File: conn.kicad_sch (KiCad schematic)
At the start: 31 parts, among them J1 JST_1x02, J10 MicroFit_2x04, J11 MLX_1x03, J12 MLX_1x03, J13 JST_1x04, J14 JST_1x04, J15 JST_1x04, J16 JST_1x04, J17 JST_1x02, J7 JST_B6B-XH, J8 MicroFit_2x04, J9 MicroFit_2x04, SW2 !EMERG STOP!

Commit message: Lots of changes and errors fixed. Updated vanity images.
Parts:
- added J5: JST_01x02, Connector_JST:JST_EH_B2B-EH-A_1x02_P2.50mm_Vertical, symbol Connector_Generic:Conn_01x02
- added NT3, NT9: DNI, _footprints:NetTie-2_SMD_Pad0.3mm, symbol Device:NetTie_2
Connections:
- net P1_OUT renamed XMIN_OUT
- net P2_OUT renamed YMIN_OUT
- net P3_OUT renamed ZMIN_OUT
- net P4_OUT renamed PROBE_OUT
- new net P16_IN: NT3.1
- new net P16_OUT: J5.1 (Pin_1), NT3.2
- new net P17_IN: NT9.1
- new net P17_OUT: J5.2 (Pin_2), NT9.2
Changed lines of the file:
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@@
     (rev "1.0")
+  )
+  (junction (at 215.9 82.55) (diameter 0) (color 0 0 0 0)
+  )
+  (junction (at 215.9 85.09) (diameter 0) (color 0 0 0 0)
   )
   (no_connect (at 162.56 52.07))
@@
     (stroke (width 0) (type default) (color 0 0 0 0))
   )
+  (wire (pts (xy 215.9 80.01) (xy 215.9 82.55))
+    (stroke (width 0) (type default) (color 0 0 0 0))
+  )
   (wire (pts (xy 182.245 58.42) (xy 182.245 57.15))
     (stroke (width 0) (type default) (color 0 0 0 0))
@@
     (stroke (width 0) (type default) (color 0 0 0 0))
   )
+  (wire (pts (xy 217.17 80.01) (xy 215.9 80.01))
+    (stroke (width 0) (type default) (color 0 0 0 0))
+  )
   (wire (pts (xy 56.515 77.47) (xy 59.055 77.47))
     (stroke (width 0) (type default) (color 0 0 0 0))
@@
     (stroke (width 0) (type default) (color 0 0 0 0))
   )
+  (wire (pts (xy 215.9 85.09) (xy 218.44 85.09))
+    (stroke (width 0) (type default) (color 0 0 0 0))
+  )
   (wire (pts (xy 64.135 87.63) (xy 66.675 87.63))
     (stroke (width 0) (type default) (color 0 0 0 0))
@@
     (stroke (width 0) (type default) (color 0 0 0 0))
   )
+  (wire (pts (xy 208.28 82.55) (xy 210.82 82.55))
+    (stroke (width 0) (type default) (color 0 0 0 0))
+  )
   (wire (pts (xy 56.515 56.515) (xy 59.055 56.515))
     (stroke (width 0) (type default) (color 0 0 0 0))
@@
     (stroke (width 0) (type default) (color 0 0 0 0))
   )
+  (wire (pts (xy 208.28 85.09) (xy 210.82 85.09))
+    (stroke (width 0) (type default) (color 0 0 0 0))
+  )
   (wire (pts (xy 64.135 107.95) (xy 93.345 107.95))
     (stroke (width 0) (type default) (color 0 0 0 0))
   )
+  (wire (pts (xy 215.9 88.9) (xy 215.9 85.09))
+    (stroke (width 0) (type default) (color 0 0 0 0))
+  )
   (polyline (pts (xy 217.805 138.43) (xy 186.69 138.43))
     (stroke (width 0) (type default) (color 0 0 0 0))
@@
     (stroke (width 0) (type default) (color 0 0 0 0))
   )
+  (wire (pts (xy 217.17 88.9) (xy 215.9 88.9))
+    (stroke (width 0) (type default) (color 0 0 0 0))
+  )
   (wire (pts (xy 116.84 54.61) (xy 119.38 54.61))
     (stroke (width 0) (type default) (color 0 0 0 0))
@@
   )
   (wire (pts (xy 56.515 107.95) (xy 59.055 107.95))
+    (stroke (width 0) (type default) (color 0 0 0 0))
+  )
+  (wire (pts (xy 215.9 82.55) (xy 218.44 82.55))
     (stroke (width 0) (type default) (color 0 0 0 0))
   )
@@
     (effects (font (size 1.27 1.27)) (justify left bottom))
   )
+  (label "P16_OUT" (at 217.17 80.01 0)
+    (effects (font (size 1.27 1.27)) (justify left bottom))
+  )
   (label "XMIN" (at 66.675 51.435 0)
     (effects (font (size 1.27 1.27)) (justify left bottom))
@@
     (effects (font (size 1.27 1.27)) (justify right bottom))
   )
+  (label "P17_OUT" (at 217.17 88.9 0)
+    (effects (font (size 1.27 1.27)) (justify left bottom))
+  )
   (label "XDIR" (at 88.9 87.63 180)
     (effects (font (size 1.27 1.27)) (justify right bottom))
@@
     (effects (font (size 1.27 1.27)) (justify right))
   )
+  (hierarchical_label "P16_IN" (shape input) (at 208.28 82.55 180)
+    (effects (font (size 1.27 1.27)) (justify right))
+  )
+  (hierarchical_label "P17_IN" (shape input) (at 208.28 85.09 180)
+    (effects (font (size 1.27 1.27)) (justify right))
+  )
   (hierarchical_label "ZCLK_IN" (shape input) (at 56.515 87.63 180)
     (effects (font (size 1.27 1.27)) (justify right))
@@
     (effects (font (size 1.27 1.27)) (justify right))
   )
-  (hierarchical_label "P2_OUT" (shape output) (at 56.515 53.975 180)
+  (hierarchical_label "YMIN_OUT" (shape output) (at 56.515 53.975 180)
     (effects (font (size 1.27 1.27)) (justify right))
   )
@@
     (effects (font (size 1.27 1.27)) (justify right))
   )
-  (hierarchical_label "P3_OUT" (shape output) (at 56.515 56.515 180)
-    (effects (font (size 1.27 1.27)) (justify right))
-  )
-  (hierarchical_label "P1_OUT" (shape output) (at 56.515 51.435 180)
+  (hierarchical_label "ZMIN_OUT" (shape output) (at 56.515 56.515 180)
+    (effects (font (size 1.27 1.27)) (justify right))
+  )
+  (hierarchical_label "XMIN_OUT" (shape output) (at 56.515 51.435 180)
     (effects (font (size 1.27 1.27)) (justify right))
   )
@@
     (effects (font (size 1.27 1.27)) (justify right))
   )
-  (hierarchical_label "P4_OUT" (shape output) (at 56.515 59.055 180)
+  (hierarchical_label "PROBE_OUT" (shape output) (at 56.515 59.055 180)
     (effects (font (size 1.27 1.27)) (justify right))
   )
@@
     )
     (pin "1")
+  )
+  (symbol (lib_id "Device:NetTie_2") (at 213.36 82.55 0) (unit 1)
+    (in_bom yes) (on_board yes)
+    (property "Reference" "NT3" (id 0) (at 213.36 81.915 0)
+      (effects (font (size 0.8 0.8)))
+    )
+    (property "Value" "DNI" (id 1) (at 213.36 80.01 0)
+      (effects (font (size 1.27 1.27)) hide)
+    )
+    (property "Footprint" "_footprints:NetTie-2_SMD_Pad0.3mm" (id 2) (at 213.36 82.55 0)
+      (effects (font (size 1.27 1.27)) hide)
+    )
+    (property "Datasheet" "~" (id 3) (at 213.36 82.55 0)
+      (effects (font (size 1.27 1.27)) hide)
+    )
+    (pin "1")
+    (pin "2")
   )
   (symbol (lib_id "Device:NetTie_2") (at 61.595 51.435 0) (unit 1)
@@
     (pin "4")
   )
+  (symbol (lib_id "Connector_Generic:Conn_01x02") (at 223.52 82.55 0) (unit 1)
+    (in_bom yes) (on_board yes) (fields_autoplaced)
+    (property "Reference" "J5" (id 0) (at 226.06 83.8199 0)
+      (effects (font (size 1.27 1.27)) (justify left))
+    )
+    (property "Value" "JST_01x02" (id 1) (at 226.06 85.0899 0)
+      (effects (font (size 1.27 1.27)) (justify left) hide)
+    )
+    (property "Footprint" "Connector_JST:JST_EH_B2B-EH-A_1x02_P2.50mm_Vertical" (id 2) (at 223.52 82.55 0)
+      (effects (font (size 1.27 1.27)) hide)
+    )
+    (property "Datasheet" "~" (id 3) (at 223.52 82.55 0)
+      (effects (font (size 1.27 1.27)) hide)
+    )
+    (property "JLCPCB" "C474892" (id 4) (at 223.52 82.55 0)
+      (effects (font (size 1.27 1.27)) hide)
+    )
+    (property "M.Part#" "KF350-3.5-2P" (id 5) (at 223.52 82.55 0)
+      (effects (font (size 1.27 1.27)) hide)
+    )
+    (property "Manufacturer" "Cixi Kefa Elec" (id 6) (at 223.52 82.55 0)
+      (effects (font (size 1.27 1.27)) hide)
+    )
+    (pin "1")
+    (pin "2")
+  )
   (symbol (lib_id "power:GND") (at 73.66 158.115 0) (unit 1)
     (in_bom yes) (on_board yes)
@@
     (pin "1")
   )
+  (symbol (lib_id "Device:NetTie_2") (at 213.36 85.09 0) (unit 1)
+    (in_bom yes) (on_board yes)
+    (property "Reference" "NT9" (id 0) (at 213.36 84.455 0)
+      (effects (font (size 0.8 0.8)))
+    )
+    (property "Value" "DNI" (id 1) (at 213.36 82.55 0)
+      (effects (font (size 1.27 1.27)) hide)
+    )
+    (property "Footprint" "_footprints:NetTie-2_SMD_Pad0.3mm" (id 2) (at 213.36 85.09 0)
+      (effects (font (size 1.27 1.27)) hide)
+    )
+    (property "Datasheet" "~" (id 3) (at 213.36 85.09 0)
+      (effects (font (size 1.27 1.27)) hide)
+    )
+    (pin "1")
+    (pin "2")
+  )
   (symbol (lib_id "Device:NetTie_2") (at 61.595 53.975 0) (unit 1)

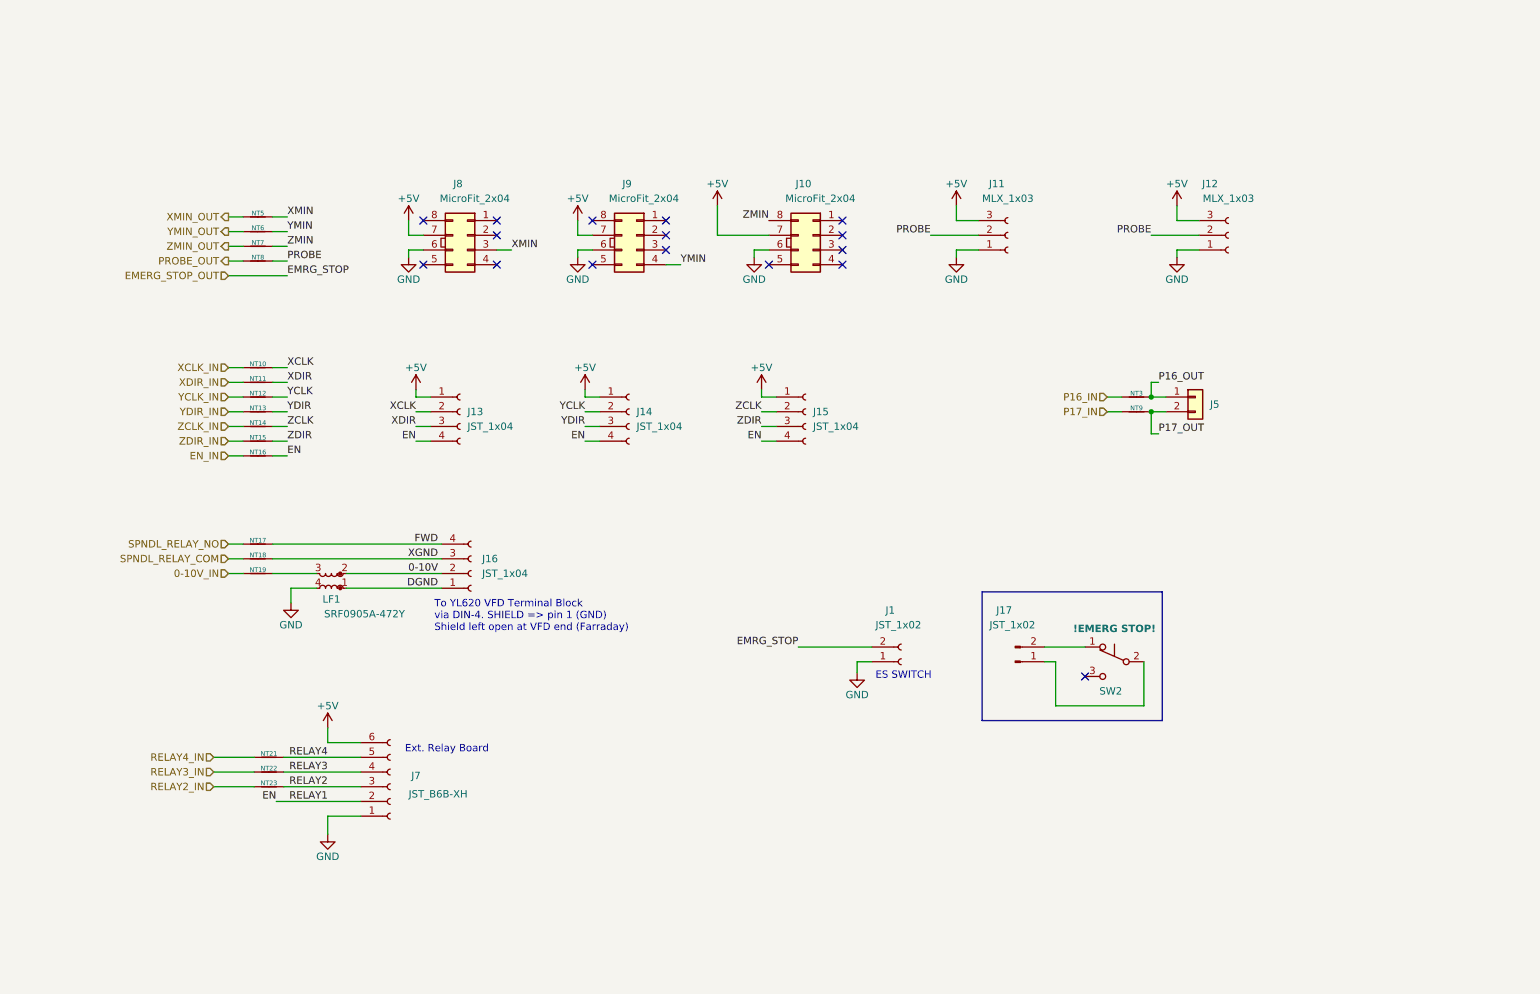
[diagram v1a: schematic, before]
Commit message: Probe connectors wired wrong. Improved 5V buck reg layout.
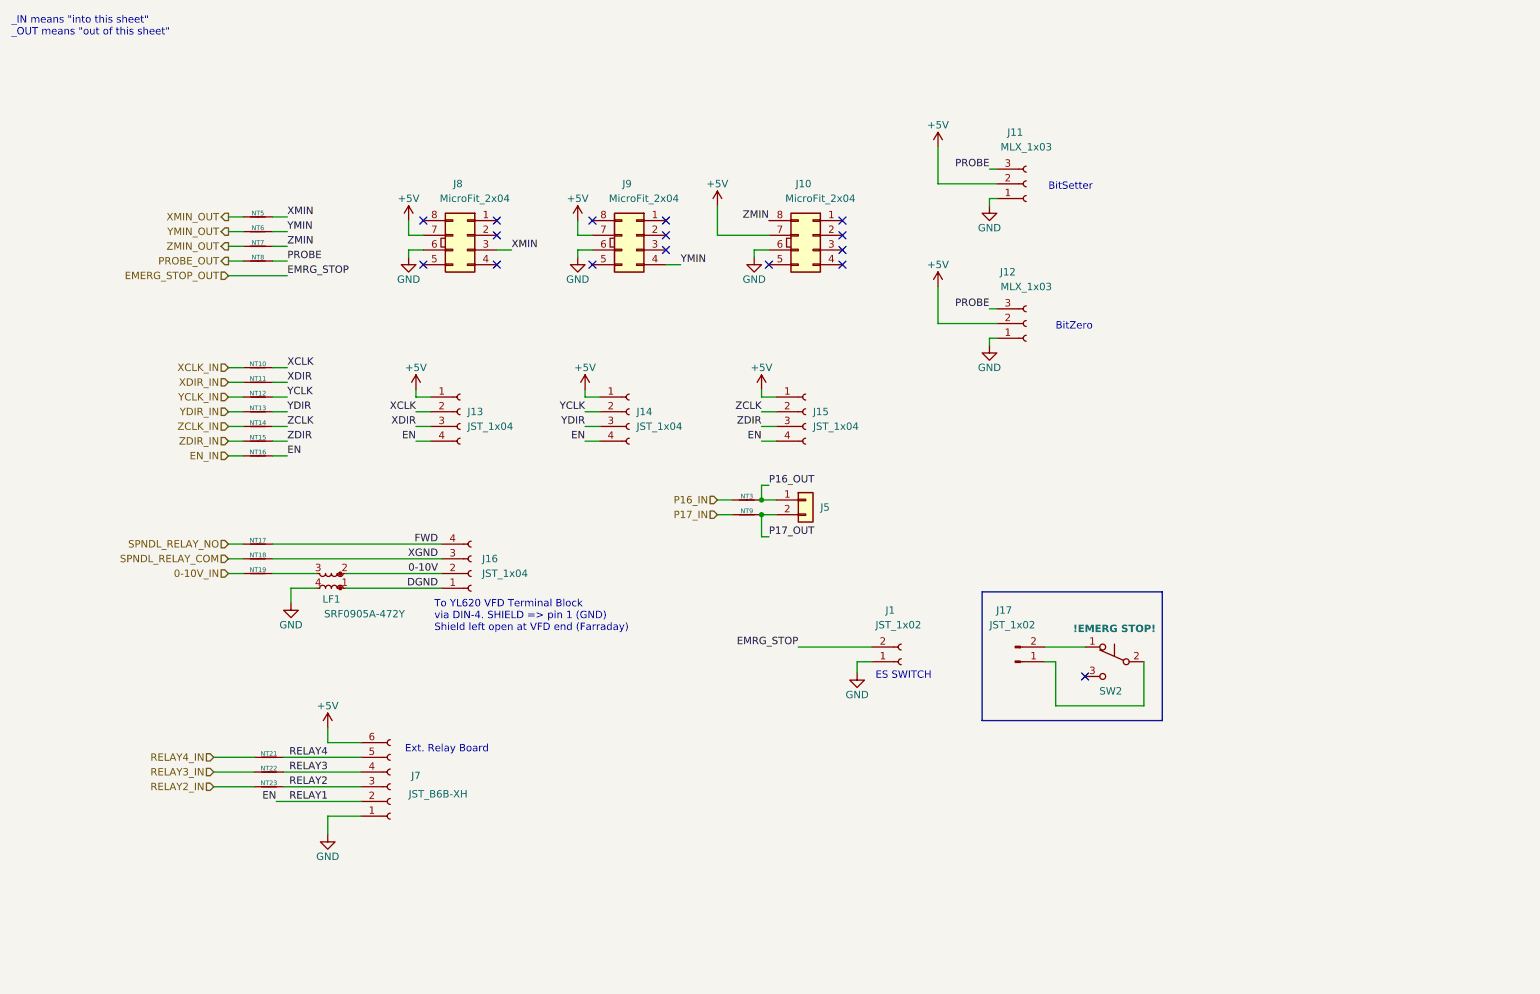
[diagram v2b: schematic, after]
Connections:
- net +5V: now also J11.2 (Pin_2), J12.2 (Pin_2); no longer J11.3 (Pin_3), J12.3 (Pin_3)
- net PROBE: now also J11.3 (Pin_3), J12.3 (Pin_3); no longer J11.2 (Pin_2), J12.2 (Pin_2)
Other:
- note added: "BitSetter"
- note added: "BitZero"
- note added: "_IN means "into this sheet" _OUT means "out of this sheet""
- moved on the sheet: J11, J12, J5, NT3, NT9

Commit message: WIP
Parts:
- added D10, D14, D6: ORG, LED_SMD:LED_0402_1005Metric, symbol Device:LED
- added D11, D15, D7: BLU, LED_SMD:LED_0402_1005Metric, symbol Device:LED
- added D12, D16, D20, D8: RED, LED_SMD:LED_0402_1005Metric, symbol Device:LED
- added D13, D5, D9: GRN, LED_SMD:LED_0402_1005Metric, symbol Device:LED
- added D17, D18, D19: (no value), LED_SMD:LED_0402_1005Metric, symbol Device:LED
- added NT1, NT20, NT4: DNI, _footprints:NetTie-2_SMD_Pad1.0mm, symbol Device:NetTie_2
- added RN5, RN6, RN7, RN8: 1Kx4, Resistor_SMD:R_Array_Convex_4x0402, symbol Device:R_Pack04
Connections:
- net +5V: now also NT1.2, NT20.2, NT4.2; no longer J10.7 (Pin_7), J13.1 (Pin_1), J14.1 (Pin_1), J15.1 (Pin_1), J7.6 (Pin_6), J8.7 (Pin_7), J9.7 (Pin_7)
- net EN: now also D13.1 (K), D20.1 (K), D5.1 (K), D9.1 (K)
- net GND: now also D12.1 (K), D16.1 (K), D8.1 (K)
- net RELAY2: now also D19.1 (K)
- net RELAY3: now also D18.1 (K)
- net RELAY4: now also D17.1 (K)
- net XCLK_IN: now also D11.1 (K)
- net XDIR_IN: now also D10.1 (K)
- net YCLK_IN: now also D7.1 (K)
- net YDIR_IN: now also D6.1 (K)
- net ZCLK_IN: now also D15.1 (K)
- net ZDIR_IN: now also D14.1 (K)
- new net: D19.2 (A), RN8.2 (R2.1)
- new net: D17.2 (A), RN8.4 (R4.1)
- new net: D10.2 (A), RN6.3 (R3.1)
- new net: D13.2 (A), RN7.4 (R4.1)
- new net: J10.7 (Pin_7), J8.7 (Pin_7), J9.7 (Pin_7), NT1.1
- new net: D18.2 (A), RN8.3 (R3.1)
- new net: D9.2 (A), RN6.4 (R4.1)
- new net: D16.2 (A), RN7.1 (R1.1)
- new net: D15.2 (A), RN7.2 (R2.1)
- new net: D14.2 (A), RN7.3 (R3.1)
- new net: D8.2 (A), RN5.1 (R1.1)
- new net: D7.2 (A), RN5.2 (R2.1)
- new net: D6.2 (A), RN5.3 (R3.1)
- new net: D5.2 (A), RN5.4 (R4.1)
- new net: D20.2 (A), RN8.1 (R1.1)
- new net: D11.2 (A), RN6.2 (R2.1)
- new net: D12.2 (A), RN6.1 (R1.1)
- new net RELAY_5V: J7.6 (Pin_6), NT20.1, RN8.5 (R4.2), RN8.6 (R3.2), RN8.7 (R2.2), RN8.8 (R1.2)
- new net STEPPER_5V: J13.1 (Pin_1), J14.1 (Pin_1), J15.1 (Pin_1), NT4.1, RN5.5 (R4.2), RN5.6 (R3.2), RN5.7 (R2.2), RN5.8 (R1.2), RN6.5 (R4.2), RN6.6 (R3.2), RN6.7 (R2.2), RN6.8 (R1.2), RN7.5 (R4.2), RN7.6 (R3.2), RN7.7 (R2.2), RN7.8 (R1.2)
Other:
- moved on the sheet: J7, NT21, NT22, NT23

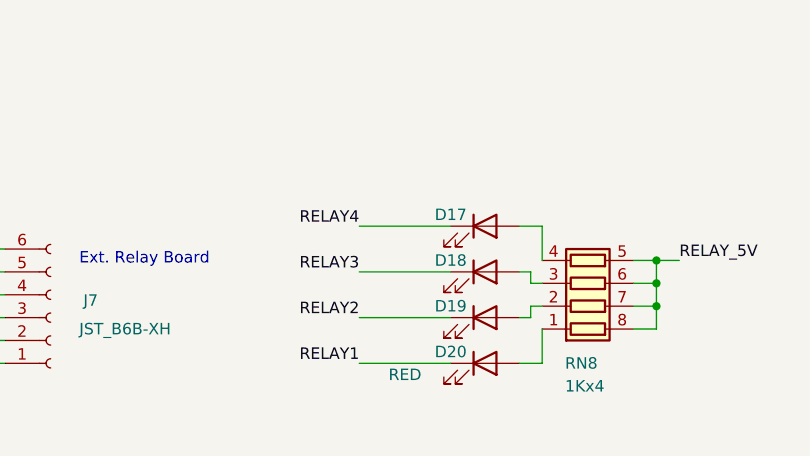
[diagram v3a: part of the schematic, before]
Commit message: Added LEDs (more coming). Changes to charge pump and related power switching.
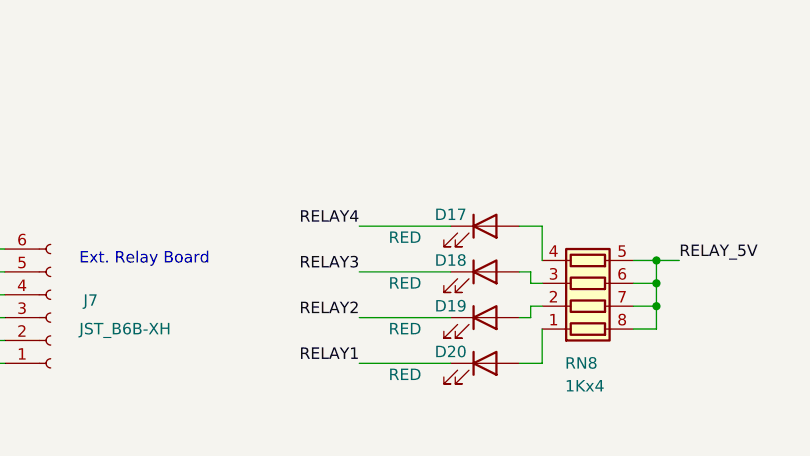
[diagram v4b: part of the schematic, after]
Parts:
- D17, D18, D19: value (none) -> RED
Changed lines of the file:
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@@
     (in_bom yes) (on_board yes)
     (property "Reference" "D19" (id 0) (at 115.57 168.91 0))
-    (property "Value" "" (id 1) (at 110.49 171.45 0))
+    (property "Value" "RED" (id 1) (at 110.49 171.45 0))
     (property "Footprint" "LED_SMD:LED_0402_1005Metric" (id 2) (at 119.38 170.18 0)
       (effects (font (size 1.27 1.27)) hide)
@@
     (in_bom yes) (on_board yes)
     (property "Reference" "D17" (id 0) (at 115.57 158.75 0))
-    (property "Value" "" (id 1) (at 110.49 161.29 0))
+    (property "Value" "RED" (id 1) (at 110.49 161.29 0))
     (property "Footprint" "LED_SMD:LED_0402_1005Metric" (id 2) (at 119.38 160.02 0)
       (effects (font (size 1.27 1.27)) hide)
@@
     (in_bom yes) (on_board yes)
     (property "Reference" "D18" (id 0) (at 115.57 163.83 0))
-    (property "Value" "" (id 1) (at 110.49 166.37 0))
+    (property "Value" "RED" (id 1) (at 110.49 166.37 0))
     (property "Footprint" "LED_SMD:LED_0402_1005Metric" (id 2) (at 119.38 165.1 0)
       (effects (font (size 1.27 1.27)) hide)

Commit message: Forgot R1 and more NT fun.
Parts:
- added NT24, NT25: DNI, _footprints:NetTie-2_SMD_Pad0.3mm, symbol Device:NetTie_2
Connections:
- net EMERG_STOP_OUT: now also NT24.1; no longer J1.2 (Pin_2)
- net EN: now also NT25.1; no longer D20.1 (K), J7.2 (Pin_2)
- new net EMRG_STOP: J1.2 (Pin_2), NT24.2
- new net RELAY1: D20.1 (K), J7.2 (Pin_2), NT25.2
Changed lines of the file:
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@@
+    (stroke (width 0) (type default) (color 0 0 0 0))
+  )
+  (wire (pts (xy 53.34 172.72) (xy 66.04 172.72))
     (stroke (width 0) (type default) (color 0 0 0 0))
   )
@@
     (stroke (width 0) (type default) (color 0 0 0 0))
   )
-  (wire (pts (xy 56.515 61.595) (xy 66.675 61.595))
+  (wire (pts (xy 56.515 61.595) (xy 59.055 61.595))
     (stroke (width 0) (type default) (color 0 0 0 0))
   )
@@
     (stroke (width 0) (type default) (color 0 0 0 0))
   )
+  (wire (pts (xy 46.99 172.72) (xy 48.26 172.72))
+    (stroke (width 0) (type default) (color 0 0 0 0))
+  )
   (wire (pts (xy 53.34 170.18) (xy 66.04 170.18))
     (stroke (width 0) (type default) (color 0 0 0 0))
@@
     (stroke (width 0) (type default) (color 0 0 0 0))
   )
+  (wire (pts (xy 64.135 61.595) (xy 66.675 61.595))
+    (stroke (width 0) (type default) (color 0 0 0 0))
+  )
   (wire (pts (xy 197.485 125.73) (xy 204.47 125.73))
     (stroke (width 0) (type default) (color 0 0 0 0))
@@
   )
   (wire (pts (xy 248.92 44.45) (xy 250.19 44.45))
-    (stroke (width 0) (type default) (color 0 0 0 0))
-  )
-  (wire (pts (xy 52.07 172.72) (xy 66.04 172.72))
     (stroke (width 0) (type default) (color 0 0 0 0))
   )
@@
     (effects (font (size 1.27 1.27)) (justify right bottom))
   )
-  (label "EN" (at 52.07 172.72 180)
+  (label "EN" (at 46.99 172.72 180)
     (effects (font (size 1.27 1.27)) (justify right bottom))
   )
@@
     )
     (property "Datasheet" "~" (id 3) (at 146.05 100.33 0)
+      (effects (font (size 1.27 1.27)) hide)
+    )
+    (pin "1")
+    (pin "2")
+  )
+  (symbol (lib_id "Device:NetTie_2") (at 50.8 172.72 0) (unit 1)
+    (in_bom yes) (on_board yes)
+    (property "Reference" "NT25" (id 0) (at 50.8 172.085 0)
+      (effects (font (size 0.8 0.8)))
+    )
+    (property "Value" "DNI" (id 1) (at 50.8 170.18 0)
+      (effects (font (size 1.27 1.27)) hide)
+    )
+    (property "Footprint" "_footprints:NetTie-2_SMD_Pad0.3mm" (id 2) (at 50.8 172.72 0)
+      (effects (font (size 1.27 1.27)) hide)
+    )
+    (property "Datasheet" "~" (id 3) (at 50.8 172.72 0)
       (effects (font (size 1.27 1.27)) hide)
     )
@@
       (effects (font (size 1.27 1.27)) hide)
     )
+    (pin "1")
+    (pin "2")
+  )
+  (symbol (lib_id "Device:NetTie_2") (at 61.595 61.595 0) (unit 1)
+    (in_bom yes) (on_board yes)
+    (property "Reference" "NT24" (id 0) (at 61.595 60.96 0)
+      (effects (font (size 0.8 0.8)))
+    )
+    (property "Value" "DNI" (id 1) (at 61.595 59.055 0)
+      (effects (font (size 1.27 1.27)) hide)
+    )
+    (property "Footprint" "_footprints:NetTie-2_SMD_Pad0.3mm" (id 2) (at 61.595 61.595 0)
+      (effects (font (size 1.27 1.27)) hide)
+    )
+    (property "Datasheet" "~" (id 3) (at 61.595 61.595 0)
+      (effects (font (size 1.27 1.27)) hide)
+    )
